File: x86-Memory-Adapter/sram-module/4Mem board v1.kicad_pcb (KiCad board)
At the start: 2 copper layers, 149.9 x 73.7 mm, 35 parts, among them K1 CONN_3, P1 CONN_1, P11 CONN_2X2, P2 CONN_1, P3 CONN_1, P4 CONN_1, P8 CONN_20X2, P9 CONN_20X2, U1 SRAM_128KB, U14 XC9536XL-VQ44, U2 SRAM_128KB, U3 SRAM_128KB, U4 SRAM_128KB, U7 LM1086CS_TO252_DPAK

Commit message: x86-Memory-Adapter: SRAM module routed board and gerbers
Source: S100 4GB DRAM BOARD/4Mem board v1 (GERBERS/ and '4Mem board v1.kicad_pcb-bak')
The routed board as plotted on 2015-05-02 survives only as the KiCad backup file '4Mem board v1.kicad_pcb-bak'; it is committed here renamed to '4Mem board v1.kicad_pcb'.
This board and the gerbers still contain a trial DDR3 DIMM footprint (removed in the next module commit).
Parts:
- added ^^DDR3_DIMM_240pin: VAL**, ^^DDR3_DIMM_240pin, B.Cu at (118.9, 135.9)
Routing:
- net GND: track 0.00 -> 703.0 mm, vias 0 -> 26
- net /V3.3: track 0.00 -> 371.5 mm, vias 0 -> 5
- net /mA12: track 0.00 -> 186.4 mm, vias 0 -> 2
- net /mA14: track 0.00 -> 182.0 mm, vias 0 -> 4
- net /mA18: track 0.00 -> 176.6 mm, vias 0 -> 3
- net /mA17: track 0.00 -> 165.6 mm, vias 0 -> 1
- net /mA13: track 0.00 -> 165.1 mm, vias 0 -> 3
- net /mA11: track 0.00 -> 163.8 mm, vias 0 -> 2
- net /mA10: track 0.00 -> 162.2 mm, vias 0 -> 2
- net /mA16: track 0.00 -> 158.4 mm, vias 0 -> 3
- net /mA8: track 0.00 -> 158.0 mm
- net /mA15: track 0.00 -> 156.3 mm, vias 0 -> 2
- net /mA6: track 0.00 -> 156.2 mm, vias 0 -> 1
- net /mA7: track 0.00 -> 153.5 mm, vias 0 -> 1
- net /mA5: track 0.00 -> 149.1 mm, vias 0 -> 1
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- added copper zone on B.Cu, net GND
- added copper zone on F.Cu, net GND
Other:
- board size 149.9 x 73.7 mm -> 150.4 x 75.2 mm
- board text added: "4Mbit (128K x 32)"
- board text added: "4Mbit (128K x 32) © 2015 A Burrows R1.0 1815"
- board text added: "P1 P34 P36"
- board text added: "U1"
- board text added: "U2"
- board text added: "U3"
- board text added: "U4"
- board text removed: "2 4 1 3"
- board text removed: "2-4 CPLD only 1-2 & 3-4 CPLD + FPGA"
- board text removed: "5.0V 3.3V 2.5V 1.8V 1.5V 1.2V"
- board text removed: "<- in LM7805 -> out 5.0V <- in LT3081"
- board text removed: "<- in LT3081 -> out 3.3V <- in LM1086"
- board text removed: "CPLD Pins"
- board text removed: "JTAG Chain"
- board text removed: "LT3081 Output Voltage Selector"
- board text removed: "P23 P44"
- board text removed: "U10"
- board text removed: "U11"
- board text removed: "U12"
- board text removed: "U13"
- board text removed: "U8"
- board text removed: "U9"
- board text removed: "XILINX CABLE"
- board text removed: "x86 32bit Memory Adapter Board Rev 1.0"

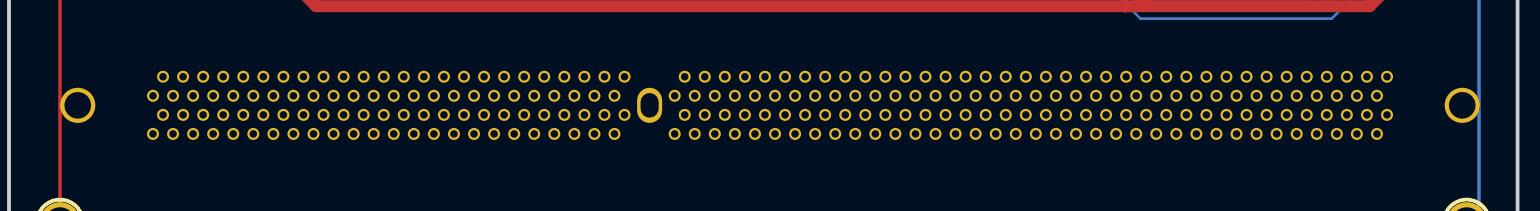
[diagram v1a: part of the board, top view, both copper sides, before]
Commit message: x86-Memory-Adapter: SRAM module trial DDR3 DIMM footprint removed
Source: S100 4GB DRAM BOARD/4Mem board v1 ('4Mem board v1.kicad_pcb' of 2015-07-12, '4Mem board v1.pro')
Routing unchanged; only the DIMM footprint was deleted.
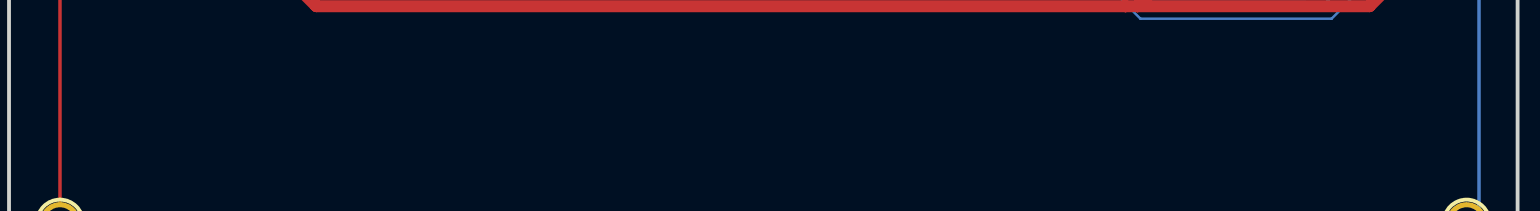
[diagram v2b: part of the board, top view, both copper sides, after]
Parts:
- removed ^^DDR3_DIMM_240pin: VAL**, ^^DDR3_DIMM_240pin
